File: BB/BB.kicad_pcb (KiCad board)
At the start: 2 copper layers, 234 parts, among them SW0 SW_Push, U1 AT90USB1286-AU, Y0 16Mhz

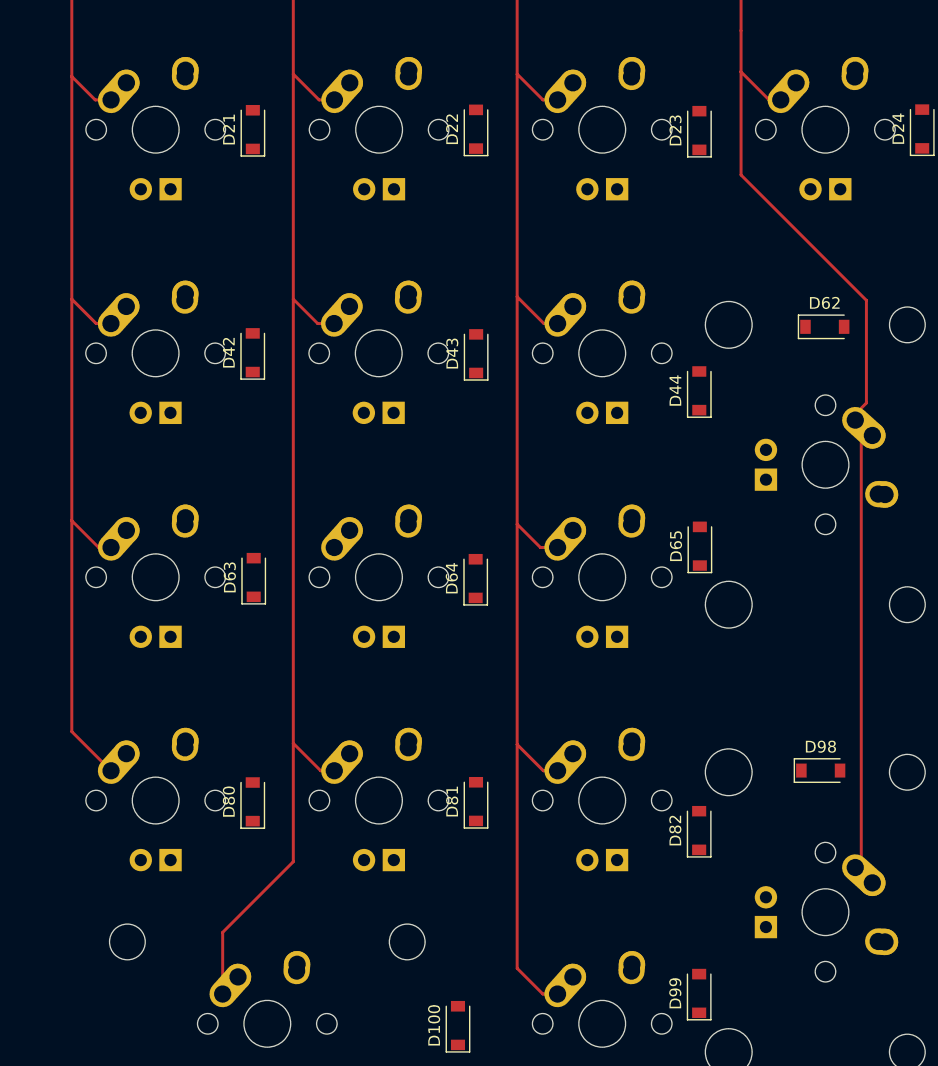
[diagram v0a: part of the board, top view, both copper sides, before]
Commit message: Finished Numpad and Alphas
Fixed numpad endings
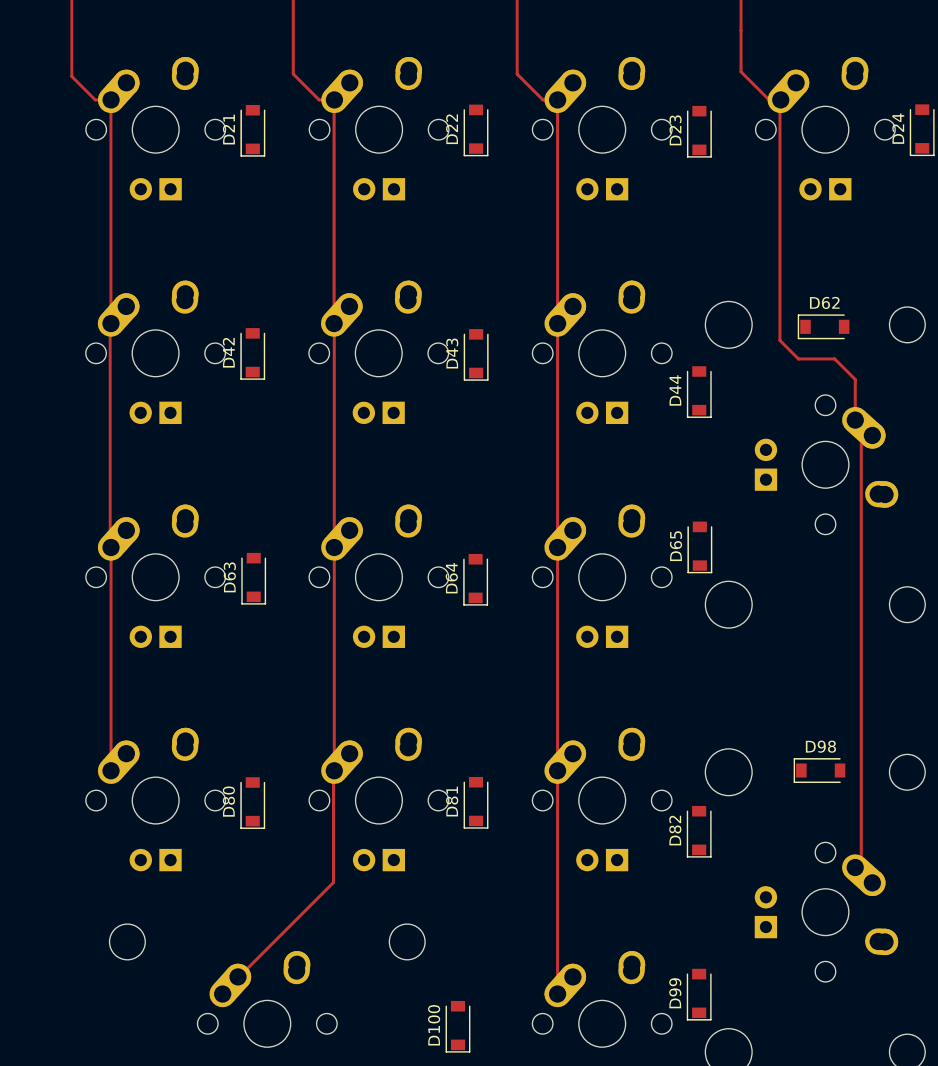
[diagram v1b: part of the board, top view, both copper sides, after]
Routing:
- net COL2: track 110.4 -> 93.0 mm
- net COL0: track 84.7 -> 72.9 mm
- net COL1: track 105.3 -> 95.8 mm
- net COL3: track 88.4 -> 85.7 mm

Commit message: Diodes with Pads
Excluding shift and keys larger than 2u on the alphas
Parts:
- moved D98 21.1 mm to (103.7, 191.6)
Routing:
- net Net-(D62-Pad2): track 0.00 -> 17.1 mm
- net Net-(D100-Pad2): track 0.00 -> 15.2 mm
- net Net-(D109-Pad2): track 0.00 -> 11.0 mm
- net Net-(D44-Pad2): track 0.00 -> 8.81 mm
- net Net-(D98-Pad2): track 0.00 -> 8.27 mm
- net Net-(D108-Pad2): track 0.00 -> 8.02 mm
- net Net-(D102-Pad2): track 0.00 -> 7.97 mm
- net Net-(D101-Pad2): track 0.00 -> 7.97 mm
- net Net-(D104-Pad2): track 0.00 -> 7.89 mm
- net Net-(D103-Pad2): track 0.00 -> 7.81 mm
- net Net-(D106-Pad2): track 0.00 -> 7.81 mm
- net Net-(D107-Pad2): track 0.00 -> 7.75 mm
- net Net-(D105-Pad2): track 0.00 -> 7.38 mm
- net Net-(D17-Pad2): track 0.00 -> 7.29 mm
- net Net-(D63-Pad2): track 0.00 -> 7.25 mm
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
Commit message: MCU Wired
No rows or colomns
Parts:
- moved R3 85.0 mm to (426.2, 145.8), turned to 90 degrees
- moved R0 83.3 mm to (404.5, 151.5), turned to 270 degrees
- moved C4 81.5 mm to (426.0, 159.7), turned to 180 degrees
- moved C3 78.4 mm to (426.0, 162.2), turned to 180 degrees
- moved C2 75.6 mm to (426.0, 164.8), turned to 180 degrees
- moved C5 74.3 mm to (412.1, 136.0)
- moved C6 74.3 mm to (420.0, 136.0)
- moved Y0 74.3 mm to (416.0, 135.9)
- moved C1 73.0 mm to (426.0, 167.4), turned to 180 degrees
- moved SW0 69.8 mm to (431.1, 140.8)
- moved C0 58.5 mm to (426.2, 149.8), turned to 270 degrees
- moved D97 8.02 mm to (382.8, 177.6)
- moved F0 4.96 mm to (150.3, 85.4), turned to 270 degrees
- moved U1 3.13 mm to (415.2, 148.5)
- moved R2 1.35 mm to (145.0, 86.0)
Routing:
- net GND: track 0.00 -> 56.8 mm
- net +5V: track 0.00 -> 19.3 mm
- net Net-(R3-Pad2): track 0.00 -> 17.5 mm
- net Net-(D38-Pad2): track 0.00 -> 14.8 mm
- net Net-(C5-Pad1): track 0.00 -> 13.1 mm
- net Net-(D67-Pad2): track 0.00 -> 12.7 mm
- net Net-(D79-Pad2): track 0.00 -> 10.9 mm
- net Net-(D86-Pad2): track 0.00 -> 10.6 mm
- net D+: track 0.00 -> 10.5 mm
- net Net-(D45-Pad2): track 0.00 -> 10.5 mm
- net Net-(D58-Pad2): track 0.00 -> 10.4 mm
- net D-: track 0.00 -> 9.99 mm
- net VCC: track 0.00 -> 9.88 mm
- net Net-(D97-Pad2): track 0.00 -> 9.00 mm
- net Net-(D82-Pad2): track 0.00 -> 8.45 mm
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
